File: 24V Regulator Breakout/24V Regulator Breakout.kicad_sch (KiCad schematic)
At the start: 9 parts, among them U1 PKE3316ZPI

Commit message: Finished Breakout Layout
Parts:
- C1: footprint (none) -> Capacitor_SMD:C_0603_1608Metric_Pad1.08x0.95mm_HandSolder
- C2: footprint (none) -> Capacitor_SMD:C_1206_3216Metric_Pad1.33x1.80mm_HandSolder
- Conn1, Conn2: footprint (none) -> MRDT_Connectors:MOLEX_SL_02_Horizontal
- U1: footprint (none) -> MRDT_Devices:PKE3316ZPI
- V1, V2, V3, V4: footprint (none) -> MRDT_Drill_Holes:4_40_Hole
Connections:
- net GND: now reaches Conn2.2, U1.1 (ON/OFF), U1.2 (VIN-)
- net GND: now also C1.1, C2.1, Conn1.1, U1.6 (VOUT-)
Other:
- moved on the sheet: C2, V1, V2, V3, V4

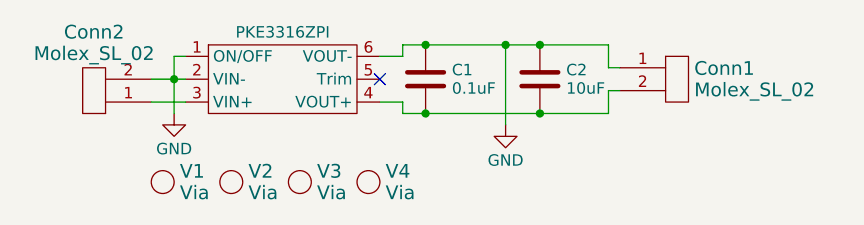
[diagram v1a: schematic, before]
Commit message: Fixed Capacitor
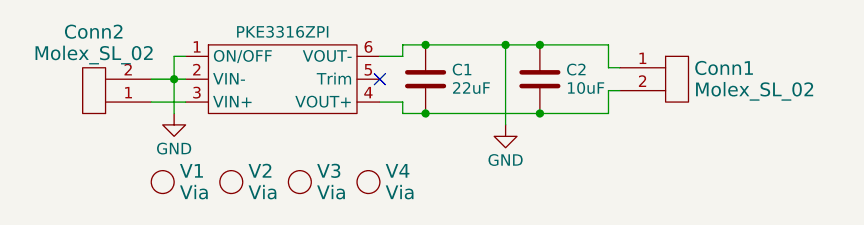
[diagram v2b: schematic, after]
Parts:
- C1: value 0.1uF -> 22uF; footprint Capacitor_SMD:C_0603_1608Metric_Pad1.08x0.95mm_HandSolder -> Capacitor_THT:CP_Radial_D5.0mm_P2.00mm
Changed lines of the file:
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@@
       (effects (font (size 1.27 1.27)) (justify left))
     )
-    (property "Value" "0.1uF" (at 109.601 54.364 0)
+    (property "Value" "22uF" (at 109.601 54.364 0)
       (effects (font (size 1.27 1.27)) (justify left))
     )
-    (property "Footprint" "Capacitor_SMD:C_0603_1608Metric_Pad1.08x0.95mm_HandSolder" (at 107.6452 57.15 0)
+    (property "Footprint" "Capacitor_THT:CP_Radial_D5.0mm_P2.00mm" (at 107.6452 57.15 0)
       (effects (font (size 1.27 1.27)) hide)
     )
